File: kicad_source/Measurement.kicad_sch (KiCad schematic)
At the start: 25 parts, among them U10 ADS1015IDGS, U11 OPA2374AIDCN, U9 OPA2374AIDCN

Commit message: updated layout
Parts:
- C31, C32, C33, C34, C35: footprint capacitors:C_0603 -> Capacitor_SMD:C_0603_1608Metric
- R25, R26, R27, R28, R29, R30, R31, R32, R33, R34, R35, R36, R37, R38, R39, R40, R41: footprint resistors:R_0603 -> Resistor_SMD:R_0603_1608Metric
- U11, U9: footprint SOIC:SOIC-8_3.9x4.9mm_Pitch1.27mm -> Package_SO:SOIC-8_3.9x4.9mm_P1.27mm
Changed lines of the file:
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@@
       (effects (font (size 1.27 1.27)) (justify left))
     )
-    (property "Footprint" "resistors:R_0603" (id 2) (at 227.33 26.67 0)
+    (property "Footprint" "Resistor_SMD:R_0603_1608Metric" (id 2) (at 227.33 26.67 0)
       (effects (font (size 1.27 1.27)) hide)
     )
@@
       (effects (font (size 1.27 1.27)) (justify left))
     )
-    (property "Footprint" "resistors:R_0603" (id 2) (at 227.33 19.05 0)
+    (property "Footprint" "Resistor_SMD:R_0603_1608Metric" (id 2) (at 227.33 19.05 0)
       (effects (font (size 1.27 1.27)) hide)
     )
@@
       (effects (font (size 1.524 1.524)) (justify left))
     )
-    (property "Footprint" "SOIC:SOIC-8_3.9x4.9mm_Pitch1.27mm" (id 2) (at 46.99 55.88 0)
+    (property "Footprint" "Package_SO:SOIC-8_3.9x4.9mm_P1.27mm" (id 2) (at 46.99 55.88 0)
       (effects (font (size 1.524 1.524)) hide)
     )
@@
       (effects (font (size 1.524 1.524)) (justify left))
     )
-    (property "Footprint" "SOIC:SOIC-8_3.9x4.9mm_Pitch1.27mm" (id 2) (at 109.22 57.15 0)
+    (property "Footprint" "Package_SO:SOIC-8_3.9x4.9mm_P1.27mm" (id 2) (at 109.22 57.15 0)
       (effects (font (size 1.524 1.524)) hide)
     )
@@
       (effects (font (size 1.524 1.524)) (justify left))
     )
-    (property "Footprint" "SOIC:SOIC-8_3.9x4.9mm_Pitch1.27mm" (id 2) (at 204.47 74.93 0)
+    (property "Footprint" "Package_SO:SOIC-8_3.9x4.9mm_P1.27mm" (id 2) (at 204.47 74.93 0)
       (effects (font (size 1.524 1.524)) hide)
     )
@@
       (effects (font (size 1.524 1.524)) (justify left))
     )
-    (property "Footprint" "SOIC:SOIC-8_3.9x4.9mm_Pitch1.27mm" (id 2) (at 204.47 116.84 0)
+    (property "Footprint" "Package_SO:SOIC-8_3.9x4.9mm_P1.27mm" (id 2) (at 204.47 116.84 0)
       (effects (font (size 1.524 1.524)) hide)
     )
@@
       (effects (font (size 1.27 1.27)) (justify left))
     )
-    (property "Footprint" "resistors:R_0603" (id 2) (at 25.4 50.8 0)
+    (property "Footprint" "Resistor_SMD:R_0603_1608Metric" (id 2) (at 25.4 50.8 0)
       (effects (font (size 1.27 1.27)) hide)
     )
@@
       (effects (font (size 1.27 1.27)) (justify left))
     )
-    (property "Footprint" "resistors:R_0603" (id 2) (at 25.4 58.42 0)
+    (property "Footprint" "Resistor_SMD:R_0603_1608Metric" (id 2) (at 25.4 58.42 0)
       (effects (font (size 1.27 1.27)) hide)
     )
@@
       (effects (font (size 1.27 1.27)) (justify left))
     )
-    (property "Footprint" "resistors:R_0603" (id 2) (at 190.5 77.47 0)
+    (property "Footprint" "Resistor_SMD:R_0603_1608Metric" (id 2) (at 190.5 77.47 0)
       (effects (font (size 1.27 1.27)) hide)
     )
@@
       (effects (font (size 1.27 1.27)) (justify left))
     )
-    (property "Footprint" "resistors:R_0603" (id 2) (at 182.88 77.47 0)
+    (property "Footprint" "Resistor_SMD:R_0603_1608Metric" (id 2) (at 182.88 77.47 0)
       (effects (font (size 1.27 1.27)) hide)
     )
@@
       (effects (font (size 1.27 1.27)) (justify left))
     )
-    (property "Footprint" "capacitors:C_0603" (id 2) (at 95.25 129.54 0)
+    (property "Footprint" "Capacitor_SMD:C_0603_1608Metric" (id 2) (at 95.25 129.54 0)
       (effects (font (size 1.27 1.27)) hide)
     )
@@
       (effects (font (size 1.27 1.27)) (justify left))
     )
-    (property "Footprint" "resistors:R_0603" (id 2) (at 182.88 72.39 0)
+    (property "Footprint" "Resistor_SMD:R_0603_1608Metric" (id 2) (at 182.88 72.39 0)
       (effects (font (size 1.27 1.27)) hide)
     )
@@
       (effects (font (size 1.27 1.27)) (justify left))
     )
-    (property "Footprint" "resistors:R_0603" (id 2) (at 199.39 63.5 0)
+    (property "Footprint" "Resistor_SMD:R_0603_1608Metric" (id 2) (at 199.39 63.5 0)
       (effects (font (size 1.27 1.27)) hide)
     )
@@
       (effects (font (size 1.27 1.27)) (justify left))
     )
-    (property "Footprint" "capacitors:C_0603" (id 2) (at 78.74 45.72 0)
+    (property "Footprint" "Capacitor_SMD:C_0603_1608Metric" (id 2) (at 78.74 45.72 0)
       (effects (font (size 1.27 1.27)) hide)
     )
@@
       (effects (font (size 1.27 1.27)) (justify left))
     )
-    (property "Footprint" "capacitors:C_0603" (id 2) (at 254 104.14 0)
+    (property "Footprint" "Capacitor_SMD:C_0603_1608Metric" (id 2) (at 254 104.14 0)
       (effects (font (size 1.27 1.27)) hide)
     )
@@
       (effects (font (size 1.27 1.27)) (justify left))
     )
-    (property "Footprint" "resistors:R_0603" (id 2) (at 190.5 119.38 0)
+    (property "Footprint" "Resistor_SMD:R_0603_1608Metric" (id 2) (at 190.5 119.38 0)
       (effects (font (size 1.27 1.27)) hide)
     )
@@
       (effects (font (size 1.27 1.27)) (justify left))
     )
-    (property "Footprint" "resistors:R_0603" (id 2) (at 182.88 119.38 0)
+    (property "Footprint" "Resistor_SMD:R_0603_1608Metric" (id 2) (at 182.88 119.38 0)
       (effects (font (size 1.27 1.27)) hide)
     )
@@
       (effects (font (size 1.27 1.27)) (justify left))
     )
-    (property "Footprint" "resistors:R_0603" (id 2) (at 182.88 114.3 0)
+    (property "Footprint" "Resistor_SMD:R_0603_1608Metric" (id 2) (at 182.88 114.3 0)
       (effects (font (size 1.27 1.27)) hide)
     )
@@
       (effects (font (size 1.27 1.27)) (justify left))
     )
-    (property "Footprint" "resistors:R_0603" (id 2) (at 199.39 105.41 0)
+    (property "Footprint" "Resistor_SMD:R_0603_1608Metric" (id 2) (at 199.39 105.41 0)
       (effects (font (size 1.27 1.27)) hide)
     )
@@
       (effects (font (size 1.27 1.27)) (justify left))
     )
-    (property "Footprint" "resistors:R_0603" (id 2) (at 91.44 156.21 0)
+    (property "Footprint" "Resistor_SMD:R_0603_1608Metric" (id 2) (at 91.44 156.21 0)
       (effects (font (size 1.27 1.27)) hide)
     )
@@
       (effects (font (size 1.27 1.27)) (justify left))
     )
-    (property "Footprint" "resistors:R_0603" (id 2) (at 48.26 137.16 0)
+    (property "Footprint" "Resistor_SMD:R_0603_1608Metric" (id 2) (at 48.26 137.16 0)
       (effects (font (size 1.27 1.27)) hide)
     )
@@
       (effects (font (size 1.27 1.27)) (justify left))
     )
-    (property "Footprint" "resistors:R_0603" (id 2) (at 50.8 144.78 0)
+    (property "Footprint" "Resistor_SMD:R_0603_1608Metric" (id 2) (at 50.8 144.78 0)
       (effects (font (size 1.27 1.27)) hide)
     )
@@
       (effects (font (size 1.27 1.27)) (justify left))
     )
-    (property "Footprint" "resistors:R_0603" (id 2) (at 137.16 146.05 0)
+    (property "Footprint" "Resistor_SMD:R_0603_1608Metric" (id 2) (at 137.16 146.05 0)
       (effects (font (size 1.27 1.27)) hide)
     )
@@
       (effects (font (size 1.27 1.27)) (justify left))
     )
-    (property "Footprint" "capacitors:C_0603" (id 2) (at 148.59 146.05 0)
+    (property "Footprint" "Capacitor_SMD:C_0603_1608Metric" (id 2) (at 148.59 146.05 0)
       (effects (font (size 1.27 1.27)) hide)
     )
@@
       (effects (font (size 1.27 1.27)) (justify left))
     )
-    (property "Footprint" "resistors:R_0603" (id 2) (at 137.16 133.35 0)
+    (property "Footprint" "Resistor_SMD:R_0603_1608Metric" (id 2) (at 137.16 133.35 0)
       (effects (font (size 1.27 1.27)) hide)
     )
@@
       (effects (font (size 1.27 1.27)) (justify left))
     )
-    (property "Footprint" "capacitors:C_0603" (id 2) (at 148.59 133.35 0)
-      (effects (font (size 1.27 1.27)) hide)
-    )
+    (property "Footprint" "Capacitor_SMD:C_0603_1608Metric" (id 2) (at 148.59 133.35 0)
+      (effects (font (size 1.27 1.27)) hide)
+    )

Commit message: added page with outputs
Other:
- title: OpenCyphalRobotController07 -> CyphalRobotController07/CAN
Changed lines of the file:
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@@
   (paper "A4")
   (title_block
-    (title "OpenCyphalRobotController07")
-    (date "2023-07-24")
+    (title "CyphalRobotController07/CAN")
+    (date "2023-10-01")
     (rev "0.1")
     (company "generationmake")

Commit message: started layout
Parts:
- removed R40: 150k, Resistor_SMD:R_0603_1608Metric, symbol Device:R_Small
- removed R41: 10k, Resistor_SMD:R_0603_1608Metric, symbol Device:R_Small
- renumbered C31 to C27, C32 to C28, C33 to C29, C34 to C30, C35 to C31, R25 to R24, R26 to R25, R27 to R26, R28 to R27, R29 to R28, R30 to R29, R31 to R30, R32 to R31, R33 to R32, R34 to R33, R35 to R34, R36 to R35, R37 to R36, R38 to R37, R39 to R38
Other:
- note removed: "factor 16 can measure up to 52.8 V"

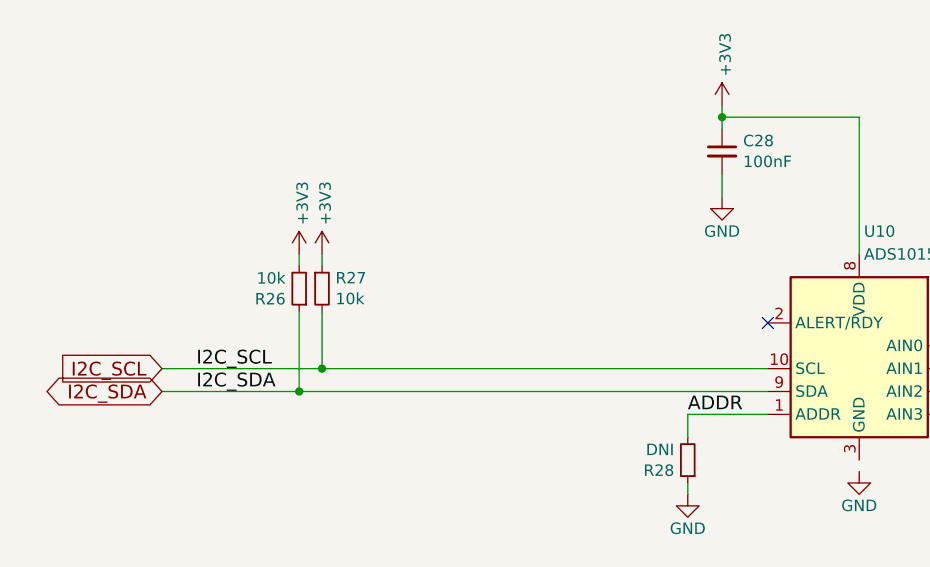
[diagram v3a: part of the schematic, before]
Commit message: made first draft of placement
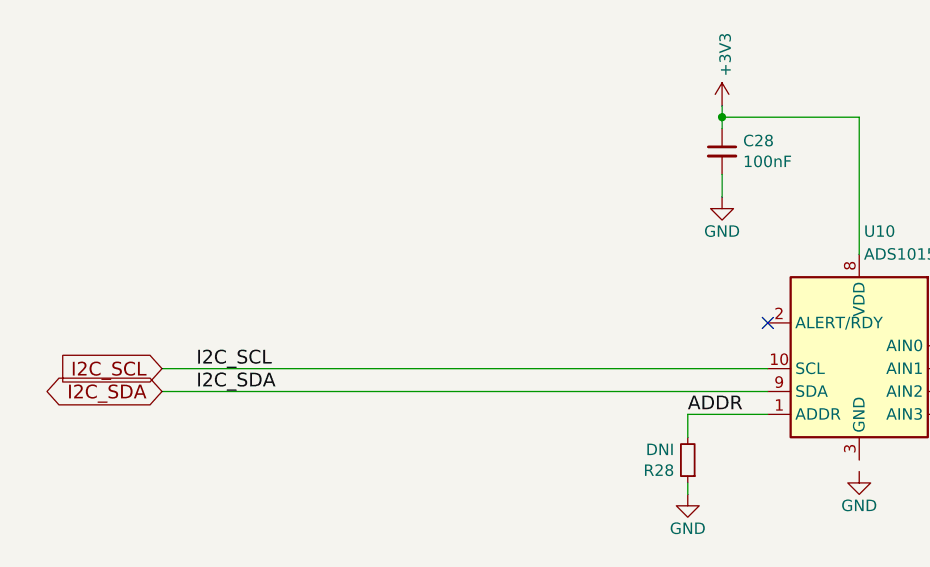
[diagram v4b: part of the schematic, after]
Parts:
- removed R26, R27: 10k, Resistor_SMD:R_0603_1608Metric, symbol Device:R_Small
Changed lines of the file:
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@@
   (junction (at 148.59 139.7) (diameter 0) (color 0 0 0 0)
-  )
-  (junction (at 48.26 152.4) (diameter 0) (color 0 0 0 0)
-  )
-  (junction (at 50.8 149.86) (diameter 0) (color 0 0 0 0)
   )
   (junction (at 148.59 127) (diameter 0) (color 0 0 0 0)
@@
     (stroke (width 0) (type default) (color 0 0 0 0))
   )
-  (wire (pts (xy 50.8 137.16) (xy 50.8 138.43))
-    (stroke (width 0) (type default) (color 0 0 0 0))
-  )
   (wire (pts (xy 163.83 119.38) (xy 176.53 119.38))
     (stroke (width 0) (type default) (color 0 0 0 0))
@@
     (stroke (width 0) (type default) (color 0 0 0 0))
   )
-  (wire (pts (xy 48.26 143.51) (xy 48.26 152.4))
-    (stroke (width 0) (type default) (color 0 0 0 0))
-  )
   (wire (pts (xy 95.25 128.27) (xy 95.25 130.81))
     (stroke (width 0) (type default) (color 0 0 0 0))
   )
-  (wire (pts (xy 48.26 152.4) (xy 100.33 152.4))
+  (wire (pts (xy 33.02 152.4) (xy 100.33 152.4))
     (stroke (width 0) (type default) (color 0 0 0 0))
   )
@@
     (stroke (width 0) (type default) (color 0 0 0 0))
   )
-  (wire (pts (xy 50.8 143.51) (xy 50.8 149.86))
-    (stroke (width 0) (type default) (color 0 0 0 0))
-  )
   (wire (pts (xy 181.61 119.38) (xy 190.5 119.38))
     (stroke (width 0) (type default) (color 0 0 0 0))
@@
     (stroke (width 0) (type default) (color 0 0 0 0))
   )
-  (wire (pts (xy 50.8 149.86) (xy 100.33 149.86))
-    (stroke (width 0) (type default) (color 0 0 0 0))
-  )
   (wire (pts (xy 201.93 86.36) (xy 201.93 85.09))
     (stroke (width 0) (type default) (color 0 0 0 0))
@@
     (stroke (width 0) (type default) (color 0 0 0 0))
   )
-  (wire (pts (xy 33.02 152.4) (xy 48.26 152.4))
-    (stroke (width 0) (type default) (color 0 0 0 0))
-  )
   (wire (pts (xy 127 149.86) (xy 127 139.7))
     (stroke (width 0) (type default) (color 0 0 0 0))
@@
     (stroke (width 0) (type default) (color 0 0 0 0))
   )
-  (wire (pts (xy 33.02 149.86) (xy 50.8 149.86))
+  (wire (pts (xy 33.02 149.86) (xy 100.33 149.86))
     (stroke (width 0) (type default) (color 0 0 0 0))
   )
@@
   )
   (wire (pts (xy 93.98 54.61) (xy 96.52 54.61))
-    (stroke (width 0) (type default) (color 0 0 0 0))
-  )
-  (wire (pts (xy 48.26 137.16) (xy 48.26 138.43))
     (stroke (width 0) (type default) (color 0 0 0 0))
   )
@@
     (pin "2")
   )
-  (symbol (lib_id "Device:R_Small") (at 48.26 140.97 180) (unit 1)
-    (in_bom yes) (on_board yes)
-    (property "Reference" "R26" (id 0) (at 46.7614 142.1384 0)
-      (effects (font (size 1.27 1.27)) (justify left))
-    )
-    (property "Value" "10k" (id 1) (at 46.7614 139.827 0)
-      (effects (font (size 1.27 1.27)) (justify left))
-    )
-    (property "Footprint" "Resistor_SMD:R_0603_1608Metric" (id 2) (at 48.26 137.16 0)
-      (effects (font (size 1.27 1.27)) hide)
-    )
-    (property "Datasheet" "" (id 3) (at 48.26 140.97 0))
-    (pin "1")
-    (pin "2")
-  )
-  (symbol (lib_id "Device:R_Small") (at 50.8 140.97 0) (unit 1)
-    (in_bom yes) (on_board yes)
-    (property "Reference" "R27" (id 0) (at 52.2986 139.8016 0)
-      (effects (font (size 1.27 1.27)) (justify left))
-    )
-    (property "Value" "10k" (id 1) (at 52.2986 142.113 0)
-      (effects (font (size 1.27 1.27)) (justify left))
-    )
-    (property "Footprint" "Resistor_SMD:R_0603_1608Metric" (id 2) (at 50.8 144.78 0)
-      (effects (font (size 1.27 1.27)) hide)
-    )
-    (property "Datasheet" "" (id 3) (at 50.8 140.97 0))
-    (pin "1")
-    (pin "2")
-  )
-  (symbol (lib_id "power:+3.3V") (at 48.26 137.16 0) (unit 1)
-    (in_bom yes) (on_board yes)
-    (property "Reference" "#PWR074" (id 0) (at 48.26 140.97 0)
-      (effects (font (size 1.27 1.27)) hide)
-    )
-    (property "Value" "+3V3" (id 1) (at 48.641 133.9088 90)
-      (effects (font (size 1.27 1.27)) (justify left))
-    )
-    (property "Footprint" "" (id 2) (at 48.26 137.16 0))
-    (property "Datasheet" "" (id 3) (at 48.26 137.16 0))
-    (pin "1")
-  )
-  (symbol (lib_id "power:+3.3V") (at 50.8 137.16 0) (unit 1)
-    (in_bom yes) (on_board yes)
-    (property "Reference" "#PWR075" (id 0) (at 50.8 140.97 0)
-      (effects (font (size 1.27 1.27)) hide)
-    )
-    (property "Value" "+3V3" (id 1) (at 51.181 133.9088 90)
-      (effects (font (size 1.27 1.27)) (justify left))
-    )
-    (property "Footprint" "" (id 2) (at 50.8 137.16 0))
-    (property "Datasheet" "" (id 3) (at 50.8 137.16 0))
-    (pin "1")
-  )
   (symbol (lib_id "Device:R_Small") (at 137.16 142.24 0) (unit 1)

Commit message: made first draft of layout
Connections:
- net GND: now also U10.3 (GND)
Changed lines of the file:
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@@
+    (stroke (width 0) (type default) (color 0 0 0 0))
+  )
+  (wire (pts (xy 110.49 160.02) (xy 110.49 161.29))
     (stroke (width 0) (type default) (color 0 0 0 0))
   )

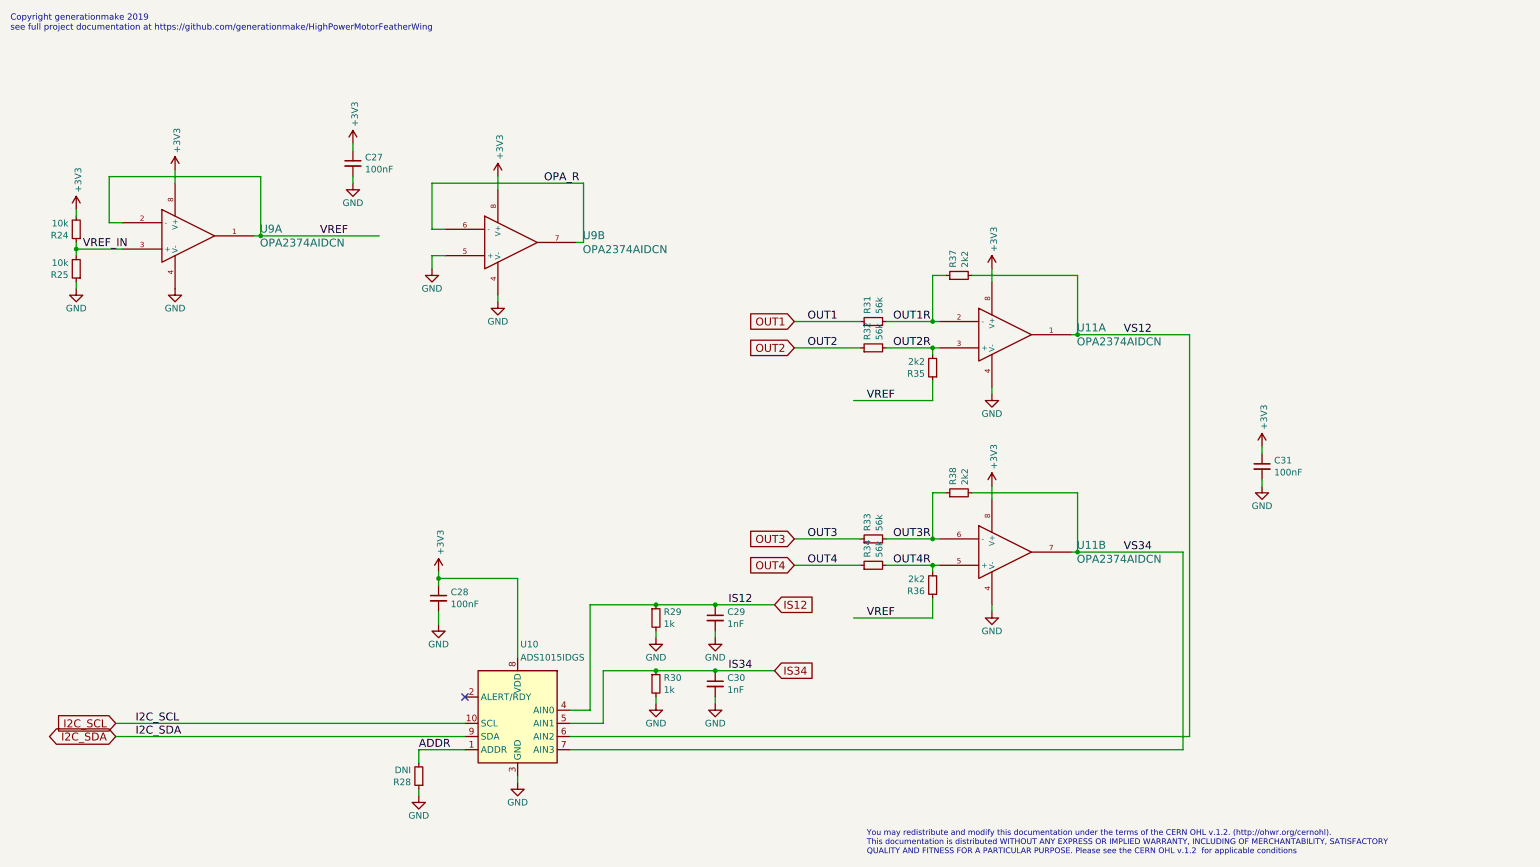
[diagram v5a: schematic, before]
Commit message: updated schematic pdf
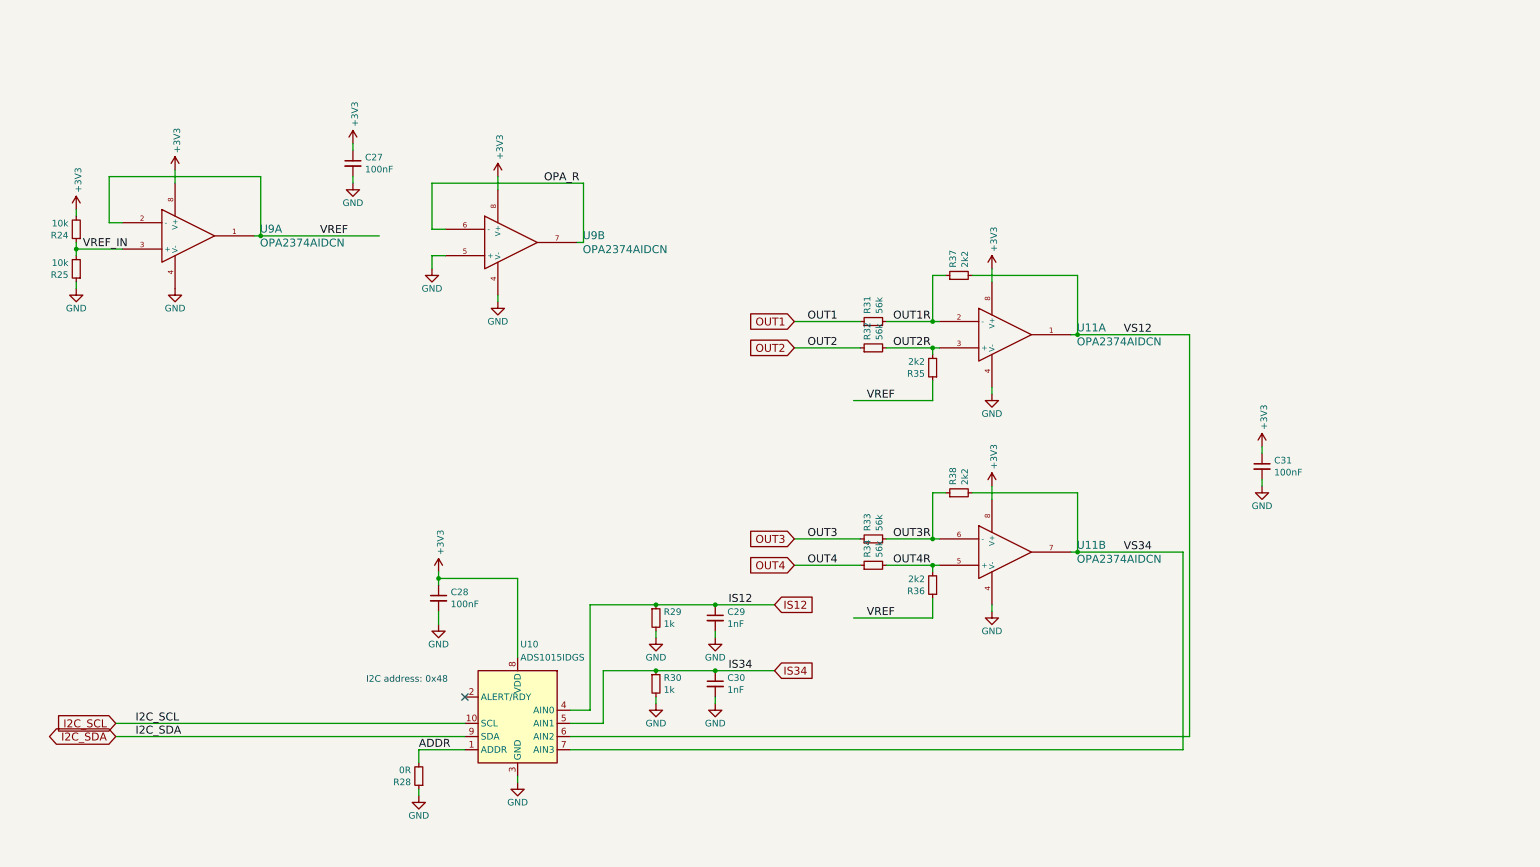
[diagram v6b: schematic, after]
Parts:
- R28: value DNI -> 0R
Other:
- note added: "I2C address: 0x48"
- note removed: "Copyright generationmake 2019 see full project documentation at https://github.com/generationmake/HighPowerMotorFeatherWing"
- note removed: "You may redistribute and modify this documentation under the terms of the CERN OHL v.1.2. (http://ohwr.org/cernohl). This documentation is distributed WITHOUT ANY EXPRESS OR IMPLIED WARRANTY, INCLUDING OF MERCHANTABILITY, SATISFACTORY QUALITY AND FITNESS FOR A PARTICULAR PURPOSE. Please see the CERN OHL v.1.2 for applicable conditions"
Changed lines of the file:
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@@
   (title_block
     (title "CyphalRobotController07/CAN")
-    (date "2023-10-01")
+    (date "2023-10-02")
     (rev "0.1")
     (company "generationmake")
@@
     (stroke (width 0) (type default) (color 0 0 0 0))
   )
-  (text "You may redistribute and modify this documentation under the terms of the CERN OHL v.1.2. (http://ohwr.org/cernohl). \nThis documentation is distributed WITHOUT ANY EXPRESS OR IMPLIED WARRANTY, INCLUDING OF MERCHANTABILITY, SATISFACTORY \nQUALITY AND FITNESS FOR A PARTICULAR PURPOSE. Please see the CERN OHL v.1.2  for applicable conditions"
-    (at 177.8 175.26 0)
-    (effects (font (size 1.0922 1.0922)) (justify left bottom))
-  )
-  (text "Copyright generationmake 2019\nsee full project documentation at https://github.com/generationmake/HighPowerMotorFeatherWing"
-    (at 12.7 16.51 0)
-    (effects (font (size 1.1938 1.1938)) (justify left bottom))
+  (text "I2C address: 0x48" (at 81.28 142.24 0)
+    (effects (font (size 1.27 1.27)) (justify left bottom))
   )
   (label "VREF" (at 177.8 87.63 0)
@@
       (effects (font (size 1.27 1.27)) (justify left))
     )
-    (property "Value" "DNI" (id 1) (at 89.9414 158.877 0)
-      (effects (font (size 1.27 1.27)) (justify left))
-    )
+    (property "Value" "0R" (id 1) (at 89.9414 158.877 0)
+      (effects (font (size 1.27 1.27)) (justify left))
+    )
